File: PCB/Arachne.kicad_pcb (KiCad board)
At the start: 2 copper layers, 100 x 70 mm, 276 parts, among them J101 Salae_logic, J102 Extension, J201 SW2, J301 SW2, J401 SW2, J501 SW2, J601 SW2, J701 SW2, J801 V_IN, J901 USB_B, J902 PROG_CONN_STM_6p, J903 DBG_UART, M201 Stepper_Motor_bipolar, M301 Stepper_Motor_bipolar, M401 Stepper_Motor_bipolar, M501 Stepper_Motor_bipolar, M601 Stepper_Motor_bipolar, M701 Stepper_Motor_bipolar, Q801 AOD4189, SW101 SW_Push, U101 STM32L452CEUx, U102 WS2818B, U201 L6470_HTSSOP28, U301 L6470_HTSSOP28, U401 L6470_HTSSOP28, U501 L6470_HTSSOP28, U601 L6470_HTSSOP28, U701 L6470_HTSSOP28, U801 ACS712xLCTR-20A, U802 NCP1117-5.0_SOT223, U803 L5973D, U804 NCP1117-3.3_SOT223, U901 USBLC6-2SC6

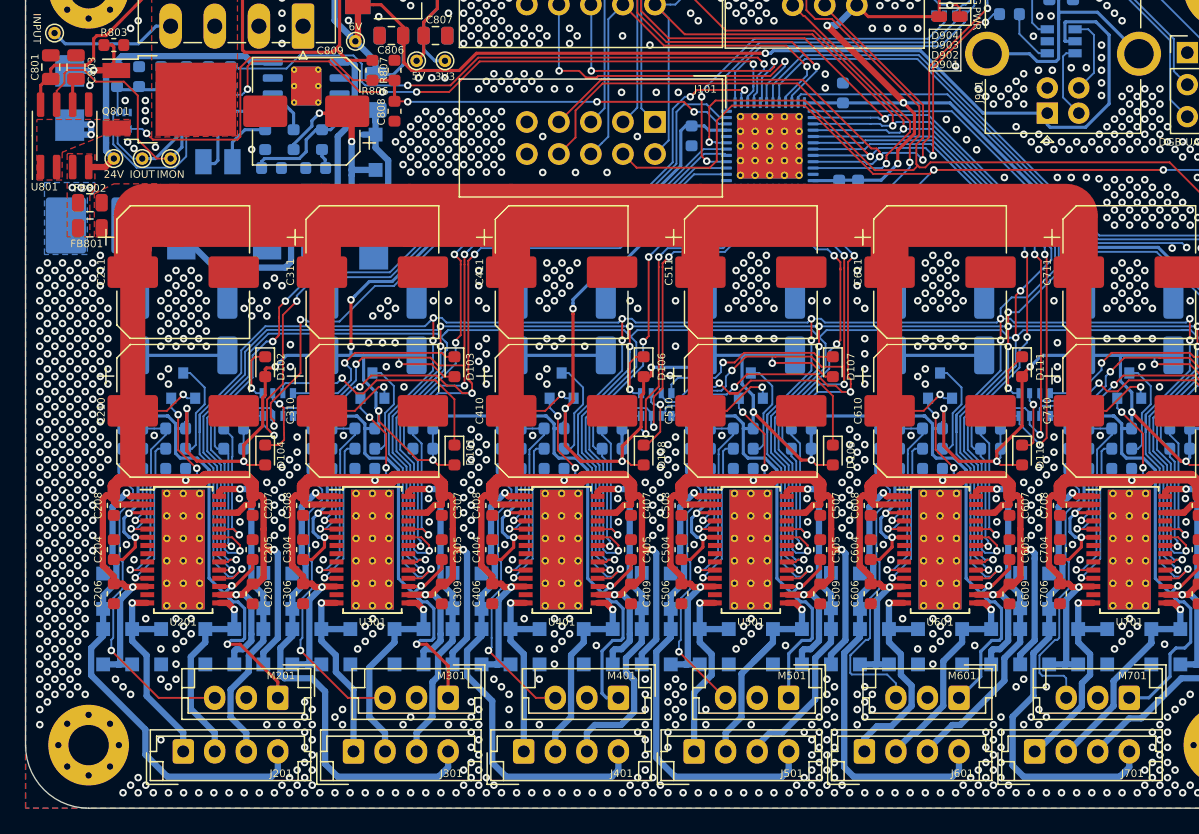
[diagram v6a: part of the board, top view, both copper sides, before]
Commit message: PCB: add info labels to silkscreen
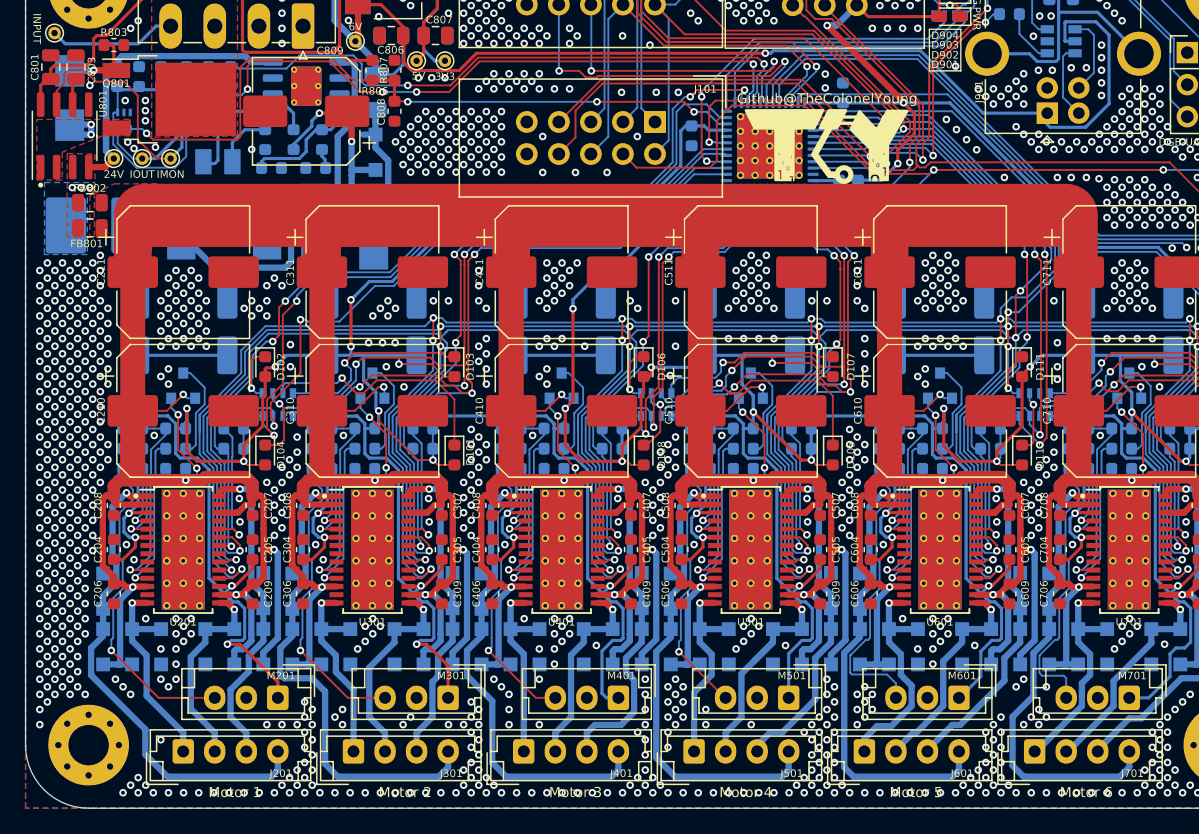
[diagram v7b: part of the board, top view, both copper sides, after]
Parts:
- added G***: LOGO, TCY_logo:TCY_QR_12x12, B.Cu at (179.7, 102.3)
- added G***: LOGO, TCY_logo:TCY_LOGO_13x6mm, F.Cu at (163.5, 97.5)
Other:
- board text added: "02/2020 v1.0"
- board text added: "3V3 GND IN"
- board text added: "A1 A2 B2 B1"
- board text added: "CLK"
- board text added: "EX_1"
- board text added: "EX_2"
- board text added: "Github@TheColonelYoung"
- board text added: "IO"
- board text added: "MISO"
- board text added: "MOSI"
- board text added: "Motor 1"
- board text added: "Motor 2"
- board text added: "Motor 3"
- board text added: "Motor 4"
- board text added: "Motor 5"
- board text added: "Motor 6"
- board text added: "NC"
- board text added: "Project ARACHNE"
- board text added: "RGB STAT"
- board text added: "RST"
- board text added: "SCK"
- board text added: "SCL"
- board text added: "SDA"
- board text added: "USD D+"
- board text added: "USD D-"
